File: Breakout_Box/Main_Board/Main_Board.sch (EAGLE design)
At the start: 18 parts, among them CN1 19PIN_LEMO

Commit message: Licenses
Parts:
- added U$1: TH-PAD-1.6/0.8, CYCFI_Con:TH-PAD-1.6/0.8
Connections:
- net AGND: now also U$1.P
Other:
- note added: "MIDI Module for Nexus Project by Cycfi Research is licensed under a Creative Commons Attribution-ShareAlike 4.0 International License. Copyright CYCFI Research Inc. 2013-2016"
- note added: "Main Board for Nexus Project by Cycfi Research is licensed under a Creative Commons Attribution-ShareAlike 4.0 International License. Copyright CYCFI Research Inc. 2013-2016"
- note removed: "Nexus Project by Cycfi Research is licensed under a Creative Commons Attribution-NonCommercial 4.0 International License. http://creativecommons.org/licenses/by-nc/4.0/ Copyright CYCFI Research Inc. 2013-2016"
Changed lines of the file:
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@@
 <part name="CN1" library="CYCFI_Con" deviceset="19PIN_LEMO" device=""/>
 <part name="D1" library="CYCFI_diode" deviceset="FM4007W" device=""/>
+<part name="U$1" library="CYCFI_Con" deviceset="TH-PAD-1.6/0.8" device=""/>
 </parts>
 <sheets>
@@
 <text x="175.26" y="86.36" size="1.778" layer="95">NC</text>
 <text x="104.14" y="86.36" size="1.778" layer="95">NC</text>
-<text x="19.05" y="10.16" size="2.54" layer="95">Nexus Project by Cycfi Research is licensed under a
-Creative Commons Attribution-NonCommercial 4.0
-International License.
-http://creativecommons.org/licenses/by-nc/4.0/
+<text x="19.05" y="10.16" size="2.54" layer="95">Main Board for Nexus Project by Cycfi Research is licensed under a Creative
+Commons Attribution-ShareAlike 4.0 International License.
 Copyright CYCFI Research Inc. 2013-2016</text>
 <text x="30.48" y="149.86" size="1.778" layer="95" rot="MR0">CH1</text>
@@
 <instance part="H13" gate="G$1" x="85.09" y="83.82" rot="R180"/>
 <instance part="CN1" gate="G$1" x="33.02" y="125.73" rot="MR180"/>
+<instance part="U$1" gate="G$1" x="33.02" y="93.98"/>
 </instances>
 <busses>
@@
 <junction x="40.64" y="104.14"/>
 <label x="30.48" y="104.14" size="1.778" layer="95" rot="MR0"/>
+<wire x1="40.64" y1="104.14" x2="40.64" y2="93.98" width="0.1524" layer="91"/>
+<pinref part="U$1" gate="G$1" pin="P"/>
+<wire x1="40.64" y1="93.98" x2="35.56" y2="93.98" width="0.1524" layer="91"/>
 </segment>
 </net>
@@
 <text x="80.01" y="125.095" size="1.778" layer="95">+12V IN</text>
 <text x="86.36" y="122.555" size="1.778" layer="95">GND</text>
-<text x="12.7" y="12.7" size="2.54" layer="95">Nexus Project by Cycfi Research is licensed under a
-Creative Commons Attribution-NonCommercial 4.0
-International License.
-http://creativecommons.org/licenses/by-nc/4.0/
+<text x="12.7" y="12.7" size="2.54" layer="95">MIDI Module for Nexus Project by Cycfi Research is licensed under a
+Creative Commons Attribution-ShareAlike 4.0 International License.
 Copyright CYCFI Research Inc. 2013-2016</text>
 <text x="200.025" y="11.43" size="2.54" layer="95">2016050</text>

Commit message: *Edit Logo *Check BOM *Added 19P Connector Files
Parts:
- renumbered U$1 to GND
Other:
- note added: "To IO Module"
- note removed: "MIDI Module for Nexus Project by Cycfi Research is licensed under a Creative Commons Attribution-ShareAlike 4.0 International License. Copyright CYCFI Research Inc. 2013-2016"
- note removed: "To Stereo Jack"

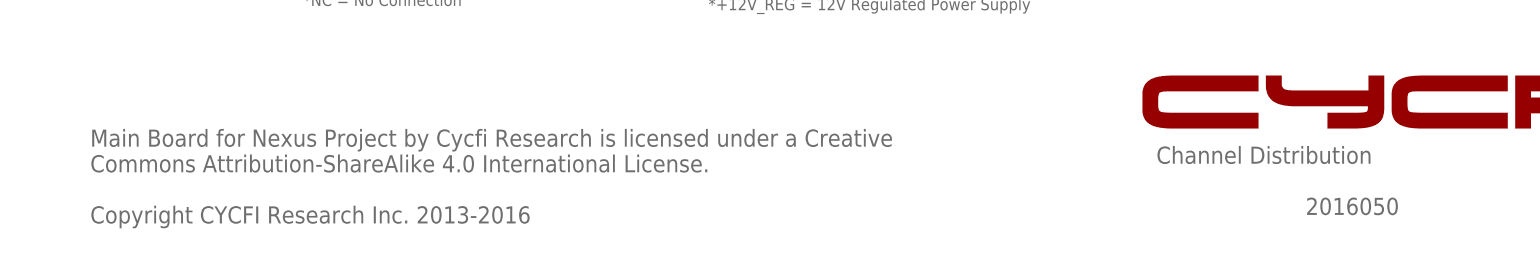
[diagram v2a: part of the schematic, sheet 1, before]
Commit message: Updated copyright and document number of schematics
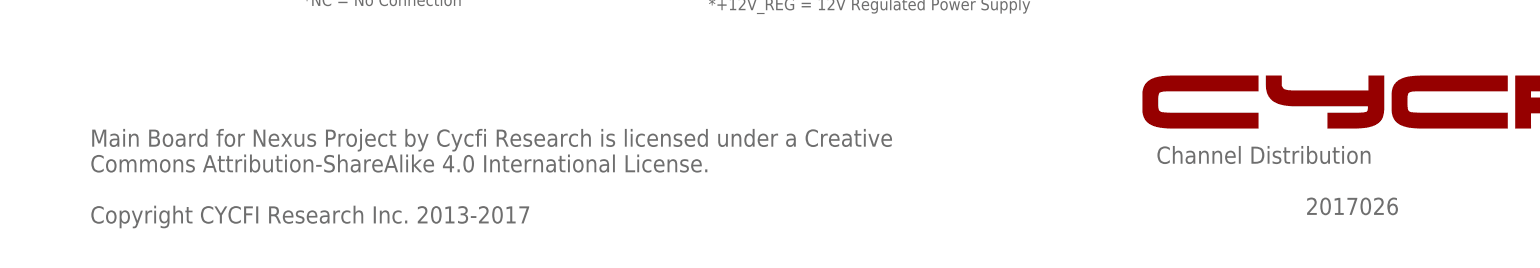
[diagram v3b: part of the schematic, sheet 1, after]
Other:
- note added: "2017026"
- note added: "Main Board for Nexus Project by Cycfi Research is licensed under a Creative Commons Attribution-ShareAlike 4.0 International License. Copyright CYCFI Research Inc. 2013-2017"
- note removed: "2016050"
- note removed: "Main Board for Nexus Project by Cycfi Research is licensed under a Creative Commons Attribution-ShareAlike 4.0 International License. Copyright CYCFI Research Inc. 2013-2016"
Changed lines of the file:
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@@
 <?xml version="1.0" encoding="utf-8"?>
 <!DOCTYPE eagle SYSTEM "eagle.dtd">
-<eagle version="6.3">
+<eagle version="7.6.0">
 <drawing>
 <settings>
@@
 <text x="177.8" y="19.05" size="2.54" layer="95">Channel Distribution</text>
 <text x="252.73" y="6.985" size="2.54" layer="95">v0.9</text>
-<text x="200.025" y="11.43" size="2.54" layer="95">2016050</text>
+<text x="200.025" y="11.43" size="2.54" layer="95">2017026</text>
 <text x="226.06" y="160.02" size="1.778" layer="95">CH1</text>
 <text x="226.06" y="157.48" size="1.778" layer="95">CH2</text>
@@
 <text x="19.05" y="10.16" size="2.54" layer="95">Main Board for Nexus Project by Cycfi Research is licensed under a Creative
 Commons Attribution-ShareAlike 4.0 International License.
-Copyright CYCFI Research Inc. 2013-2016</text>
+Copyright CYCFI Research Inc. 2013-2017</text>
 <text x="30.48" y="149.86" size="1.778" layer="95" rot="MR0">CH1</text>
 <text x="30.48" y="147.32" size="1.778" layer="95" rot="MR0">CH2</text>
@@
 <text x="12.7" y="12.7" size="2.54" layer="95">Main Board for Nexus Project by Cycfi Research is licensed under a
 Creative Commons Attribution-ShareAlike 4.0 International License.
-Copyright CYCFI Research Inc. 2013-2016</text>
-<text x="200.025" y="11.43" size="2.54" layer="95">2016050</text>
+Copyright CYCFI Research Inc. 2013-2017</text>
+<text x="200.025" y="11.43" size="2.54" layer="95">2017026</text>
 <wire x1="173.99" y1="127" x2="173.99" y2="124.46" width="0.1524" layer="95"/>
 <wire x1="173.99" y1="124.46" x2="188.595" y2="124.46" width="0.1524" layer="95"/>

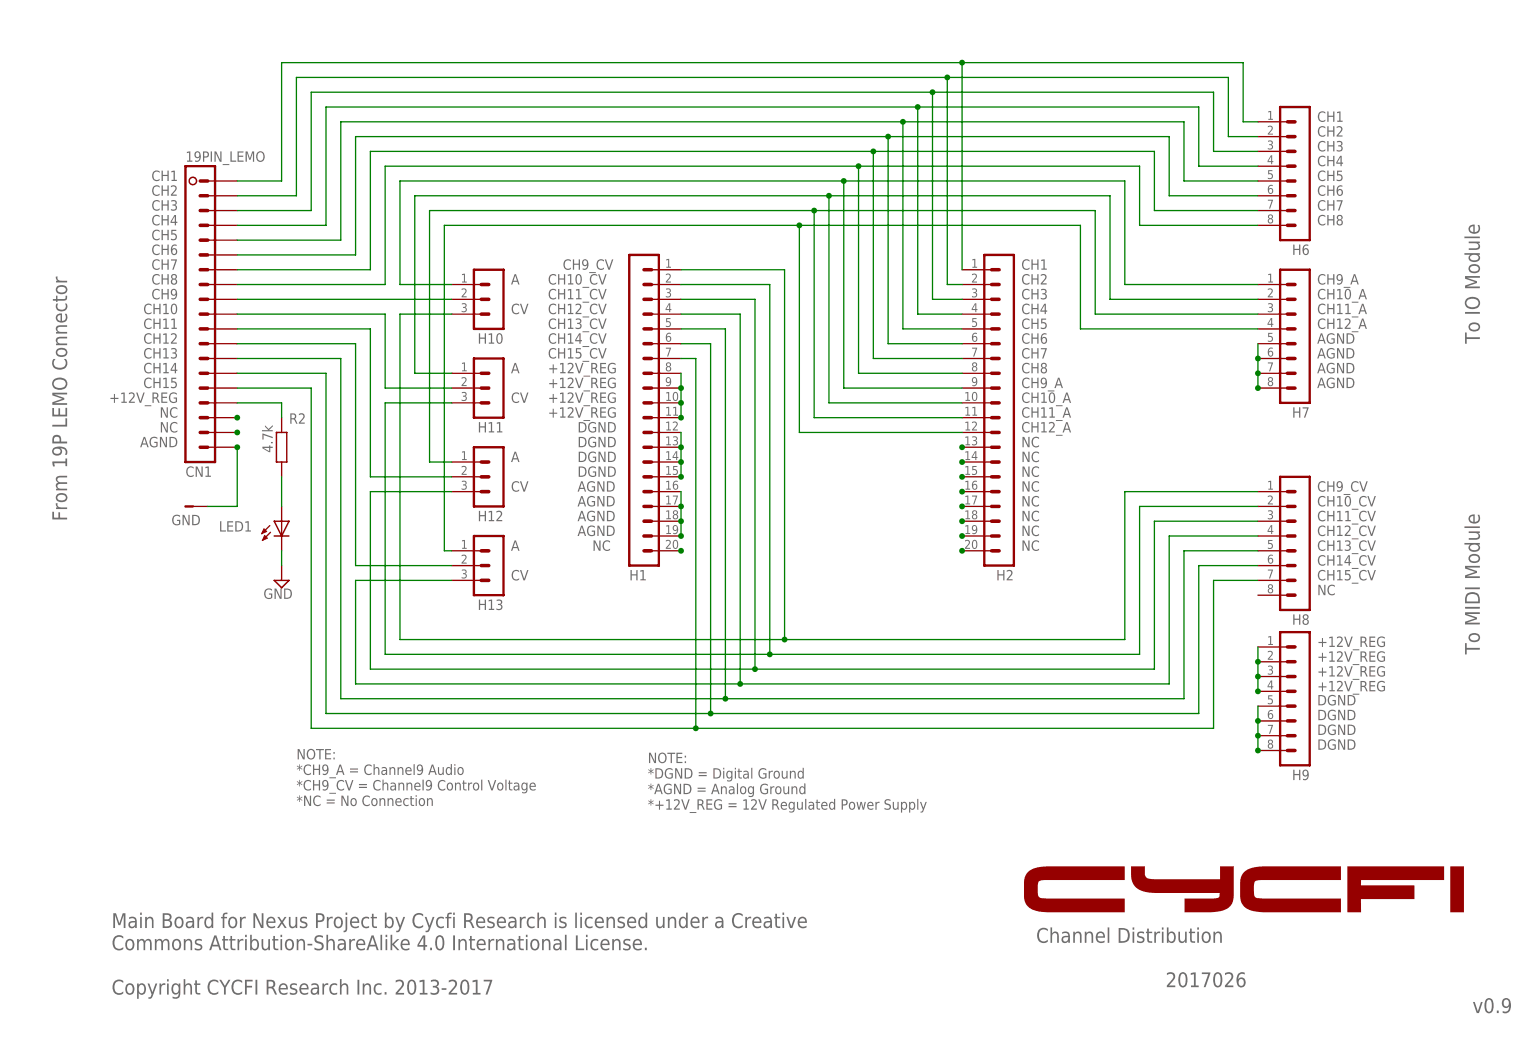
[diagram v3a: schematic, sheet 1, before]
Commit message: create version 2.1 and update main and midi modules and delete nexyus cad drawings
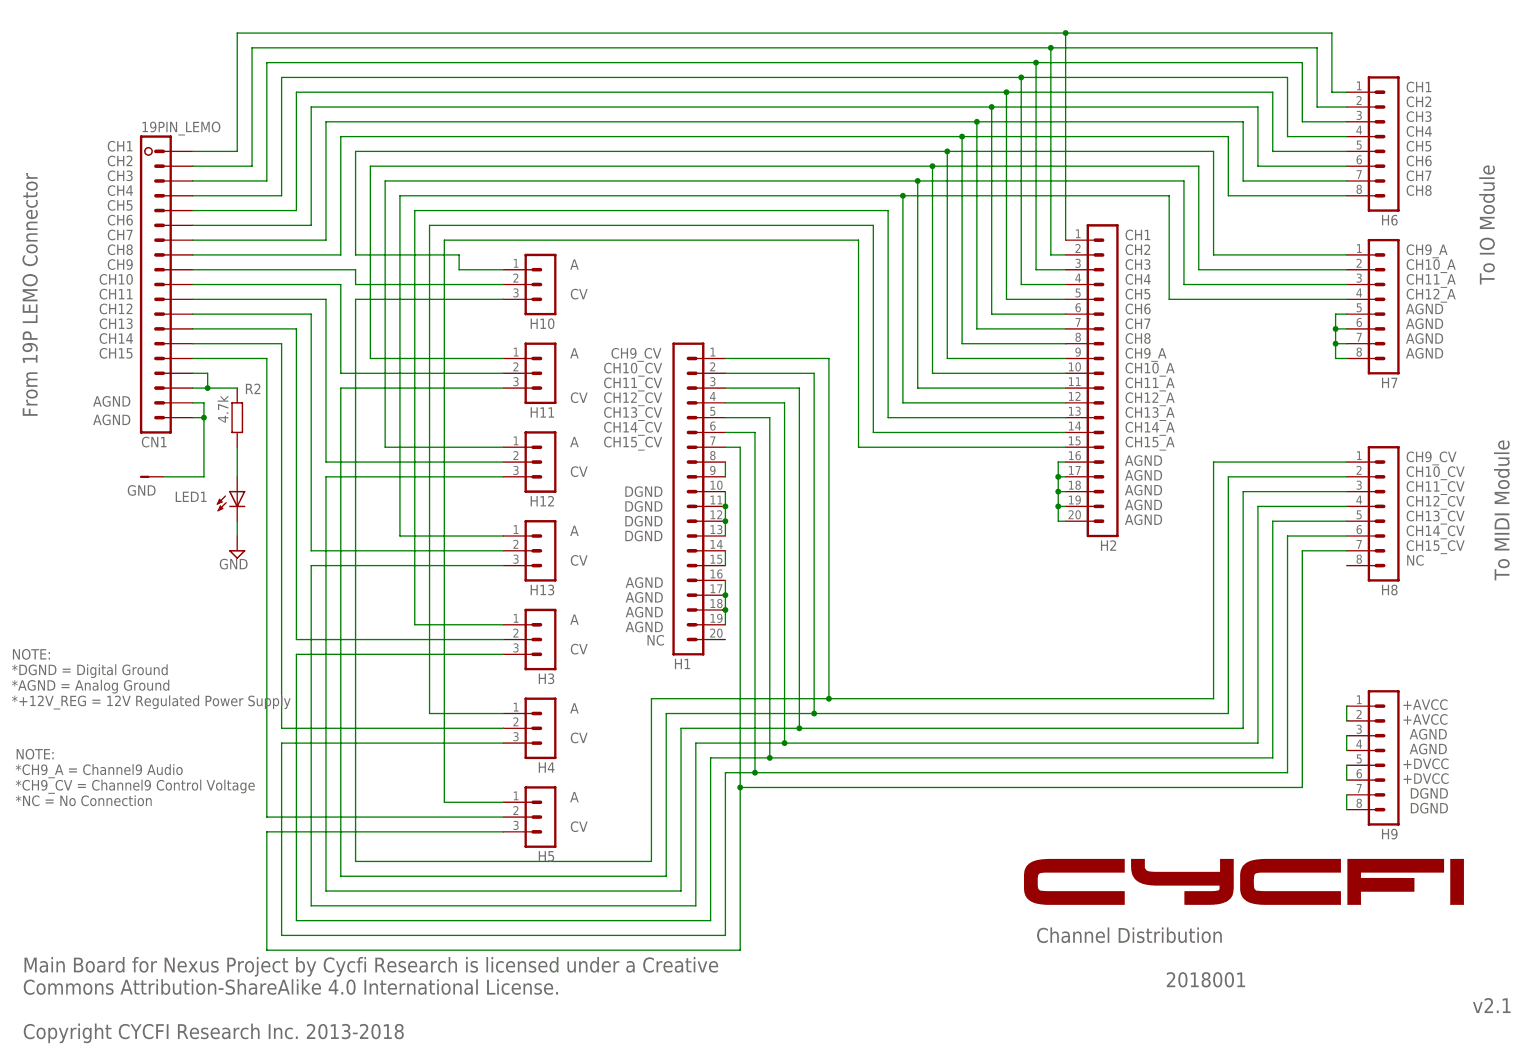
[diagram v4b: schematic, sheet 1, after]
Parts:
- added C1, C3: 22uF, resistor:C-EUC0805
- added C4: 1uF, resistor:C-EUC0603
- added C5: 10uF, resistor:C-EUC0603
- added C7: 1nF, resistor:C-EUC0402K
- added H3, H4, H5: (no value), con-lstb:MA03-1_EDITED
- added L2: 82uH, resistor:L-EU
- added Q1: DMP3099L, CYCFI_semicon:P_MOSFET
- added Q2: DSS6060, CYCFI_semicon:DSS60601MZ4-13
- added R1: 1k, resistor:R-EU_R0402
- C2: value 0.1uF -> 470uF; device resistor:C-EUC0603 -> resistor:CPOL-EU140CLH-1010
- D1: value FM4007W -> FM4004W
- L1: value 100uH -> 1mH; device resistor:L-EU -> inductors:SDR
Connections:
- removed net +12V_REG: C2.1, C6.+, CN1.16, H1.10, H1.11, H1.8, H1.9, H9.1, H9.2, H9.3, H9.4, L1.2, R2.1
- removed net AGND: C2.2, C6.-, CN1.19, GND.P, H1.16, H1.17, H1.18, H1.19, H14.1, H7.5, H7.6, H7.7, H7.8, LED1.C
- removed net DGND: H1.12, H1.13, H1.14, H1.15, H9.5, H9.6, H9.7, H9.8
- removed net N$22: H2.19
- removed net N$23: H2.20
- removed net N$24: H1.20
- removed net N$26 (its old number): CN1.18
- removed net N$31: D1.C, L1.1
- removed net N$60: CN1.13, H1.5, H8.5
- removed net N$61: CN1.14, H1.6, H8.6
- removed net N$62: CN1.15, H1.7, H8.7
- removed net N$9 (its old number): CN1.17
- new net +AVCC: C4.1, C5.1, C7.1, CN1.16, CN1.17, D1.A, H1.14, H1.15, H9.1, H9.2, Q2.E, R2.1
- new net +DVCC: C3.1, H1.8, H1.9, H9.5, H9.6, L1.2
- new net GND: C1.2, C2.-, C3.2, C4.2, C5.2, C6.-, C7.2, CN1.18, CN1.19, GND.P, H1.10, H1.11, H1.12, H1.13, H1.16, H1.17, H1.18, H1.19, H14.1, H2.16, H2.17, H2.18, H2.19, H2.20, H7.5, H7.6, H7.7, H7.8, H9.3, H9.4, H9.7, H9.8, LED1.C, Q1.G
- new net N$33: H1.5, H3.3, H8.5
- new net N$34: H1.6, H4.3, H8.6
- new net N$35: H1.7, H5.3, H8.7
- new net N$36: CN1.13, H3.2
- new net N$37: CN1.14, H4.2
- new net N$38: CN1.15, H5.2
- net N$1: now also H3.1
- net N$17: now also H5.1
- net N$19: now also C1.1, L1.1, L2.1, Q1.S; no longer H2.16
- net N$2: now also Q1.D; no longer D1.A
- net N$20: now also C2.+, Q2.B, R1.1; no longer H2.17
- net N$21: now also C6.+, D1.C, L2.2, Q2.C, R1.2; no longer H2.18
- net N$3: now also H4.1
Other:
- note added: "+AVCC"
- note added: "+DVCC"
- note added: "2018001"
- note added: "CH13_A"
- note added: "CH14_A"
- note added: "CH15_A"
- note added: "Main Board for Nexus Project by Cycfi Research is licensed under a Creative Commons Attribution-ShareAlike 4.0 International License. Copyright CYCFI Research Inc. 2013-2018"
- note added: "NOTES: *+12V_REG = 12V Regulater Power Supply for Analog * +12_VREGD = 12V Regulater Power Supply for Digital *AGND = Analog Ground *DGND= Digital Ground"
- note added: "v2.1"
- note removed: "2017026"
- note removed: "Main Board for Nexus Project by Cycfi Research is licensed under a Creative Commons Attribution-ShareAlike 4.0 International License. Copyright CYCFI Research Inc. 2013-2017"
- note removed: "NOTES: *+12V_REG = 12V Regulater Power Supply *AGND = Analog Ground *DGND= Digital Ground"
- note removed: "v0.9"
- note removed: "v0.92"
- moved on the sheet: C6, CN1, D1, GND, H1, H10, H11, H12, H13, H2, H6, H7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

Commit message: Update: Main Board MIDI Board MCU Board IO Board
Delete:
Mixer Board
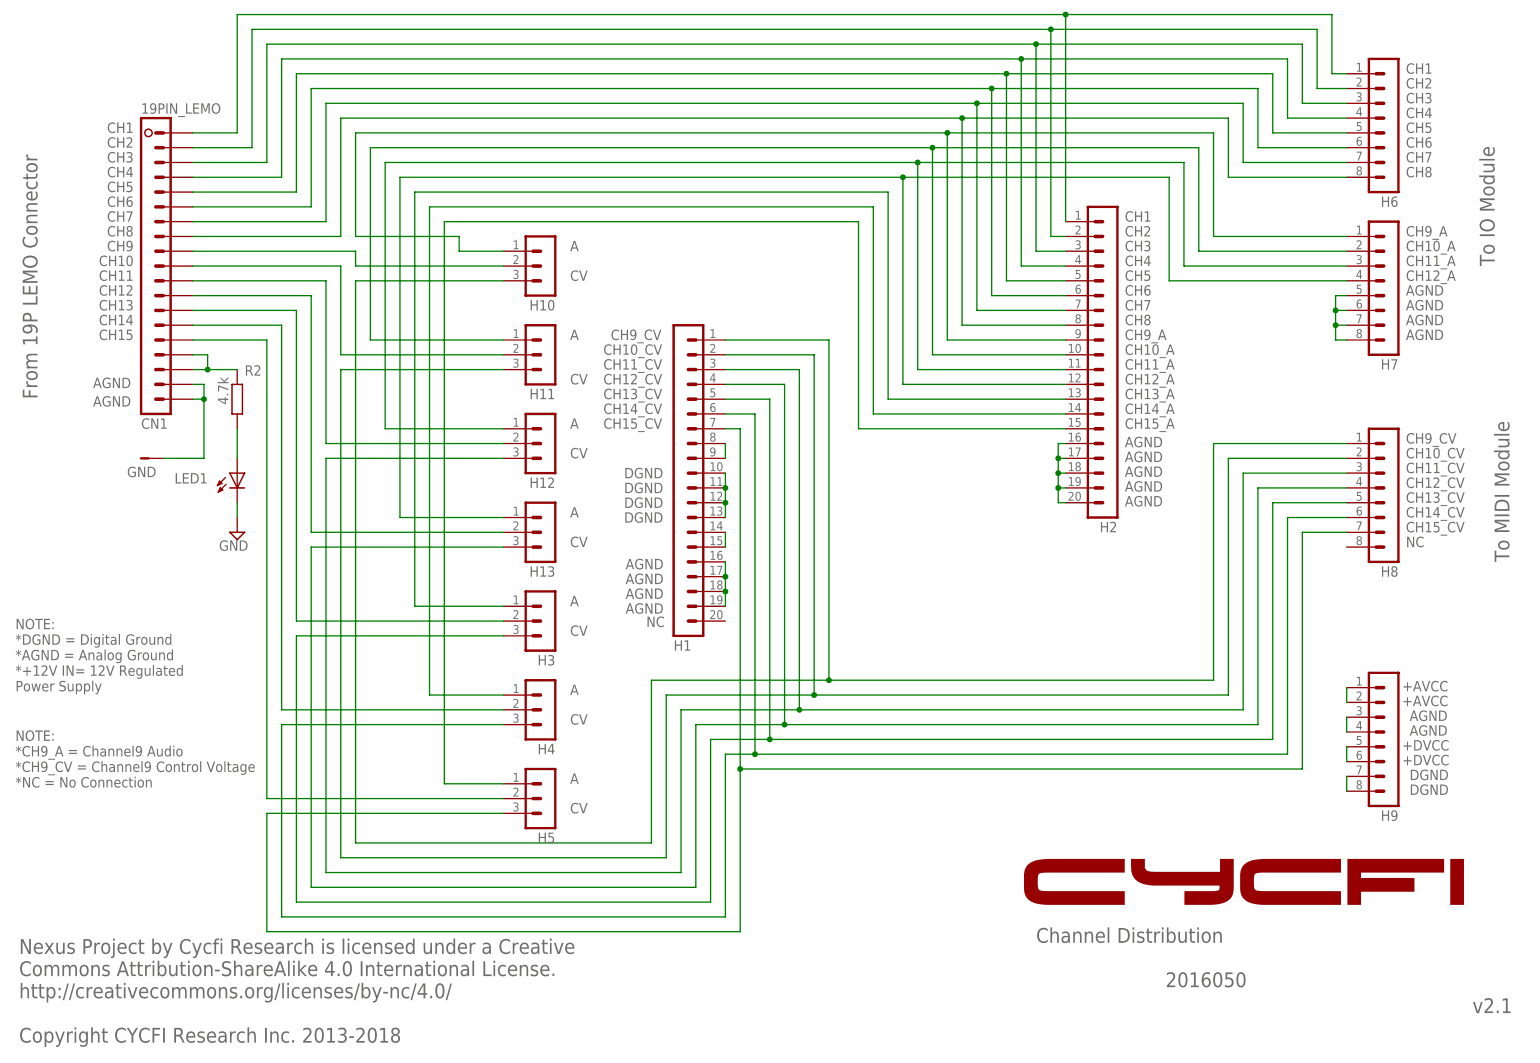
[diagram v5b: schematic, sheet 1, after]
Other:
- note added: "2016050"
- note added: "NOTE: *DGND = Digital Ground *AGND = Analog Ground *+12V IN= 12V Regulated Power Supply"
- note added: "NOTES: *+AVCC = 12V Regulater Power Supply for Analog *+DVCC = 12V Regulater Power Supply for Digital *AGND = Analog Ground *DGND= Digital Ground"
- note added: "Nexus Project by Cycfi Research is licensed under a Creative Commons Attribution-ShareAlike 4.0 International License. http://creativecommons.org/licenses/by-nc/4.0/ Copyright CYCFI Research Inc. 2013-2018"
- note removed: "2018001"
- note removed: "Main Board for Nexus Project by Cycfi Research is licensed under a Creative Commons Attribution-ShareAlike 4.0 International License. Copyright CYCFI Research Inc. 2013-2018"
- note removed: "NOTE: *DGND = Digital Ground *AGND = Analog Ground *+12V_REG = 12V Regulated Power Supply"
- note removed: "NOTES: *+12V_REG = 12V Regulater Power Supply for Analog * +12_VREGD = 12V Regulater Power Supply for Digital *AGND = Analog Ground *DGND= Digital Ground"
- moved on the sheet: CN1, GND, H1, H10, H11, H12, H13, H2, H3, H4, H5, H6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
